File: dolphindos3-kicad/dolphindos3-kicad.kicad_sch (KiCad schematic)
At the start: 23 parts, among them CN1 MB_CPU, CN2 parallel0, IC1 6502, IC10 74LS08, IC2 27256, IC3 6264, IC4 6821, IC5 74LS08, IC6 74LS08, IC7 74LS32, IC8 74LS04, IC9 74LS32

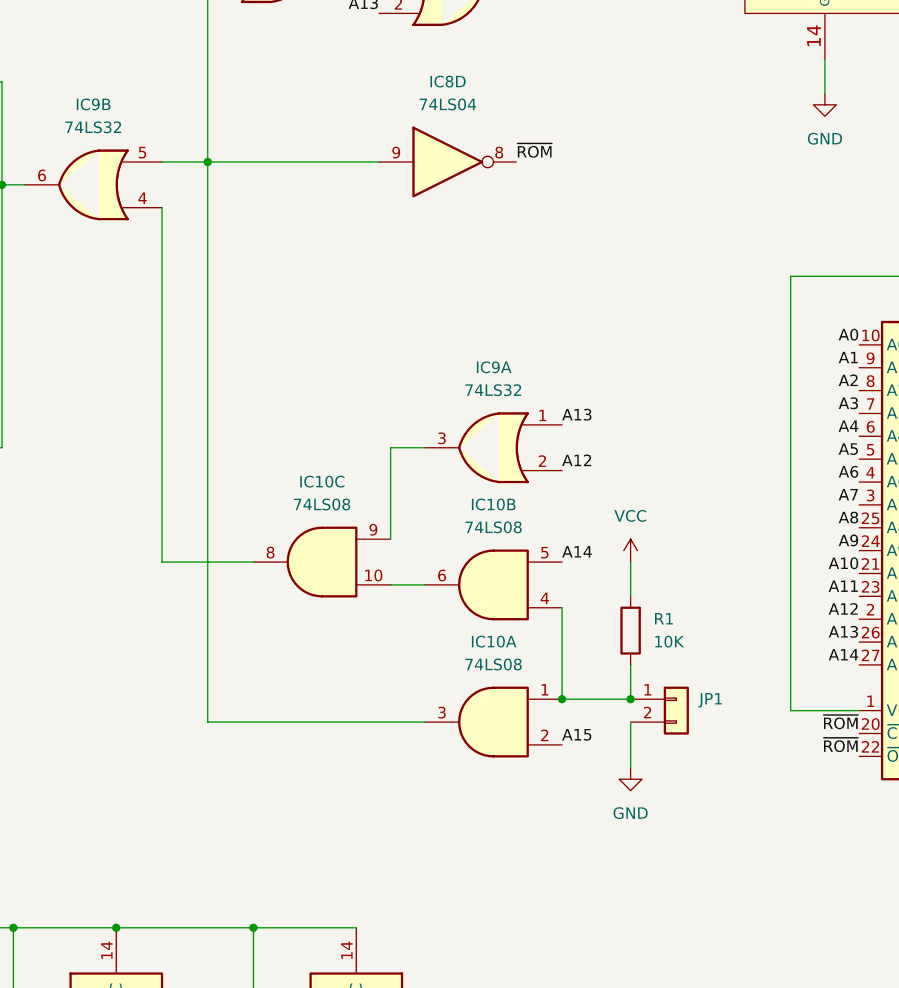
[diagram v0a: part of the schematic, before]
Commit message: redraw without crossed lines
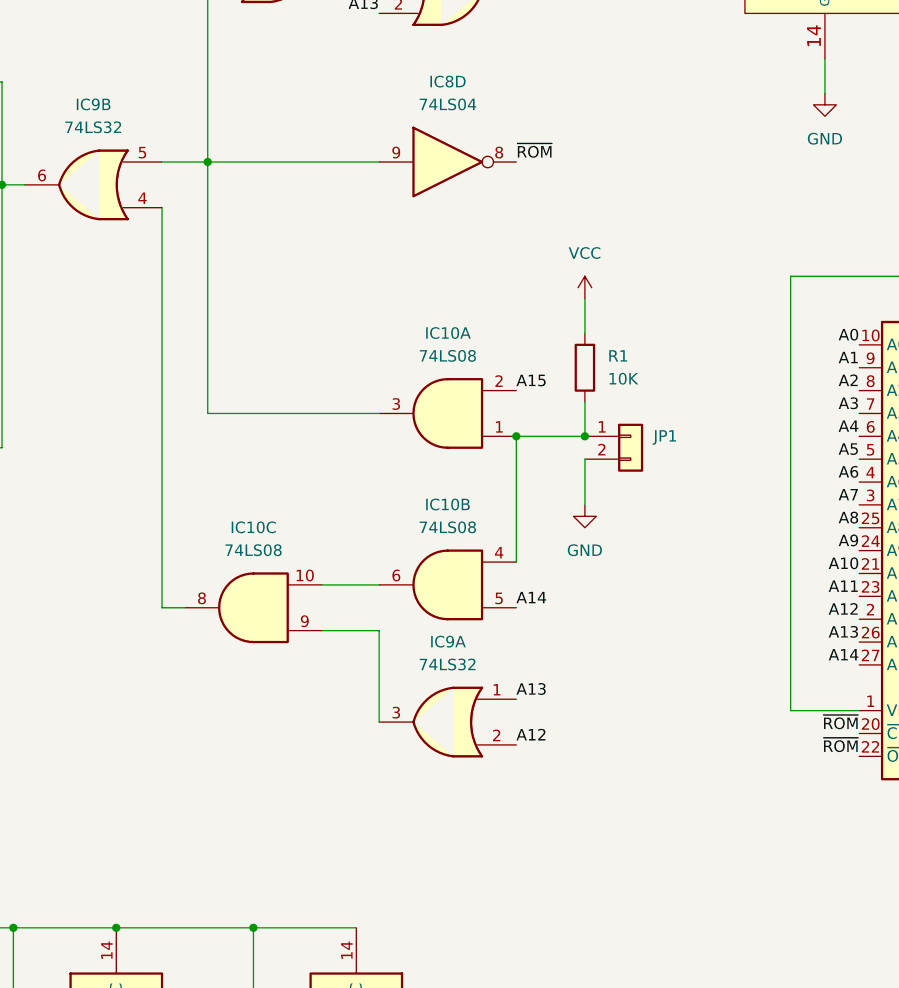
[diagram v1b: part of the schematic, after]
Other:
- moved on the sheet: IC10A, IC10B, IC10C, IC9A, JP1, R1

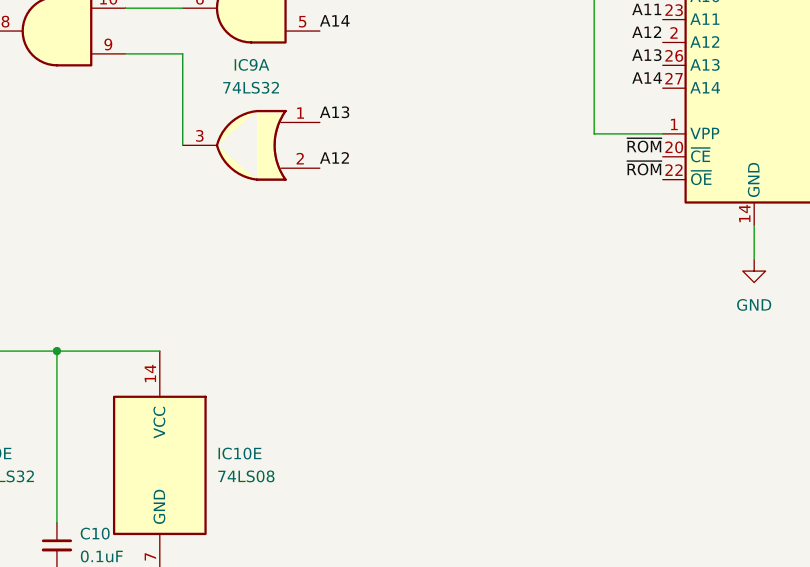
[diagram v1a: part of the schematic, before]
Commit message: IDC socket for parallel cable, added JP2 for drive reset to match gerbers
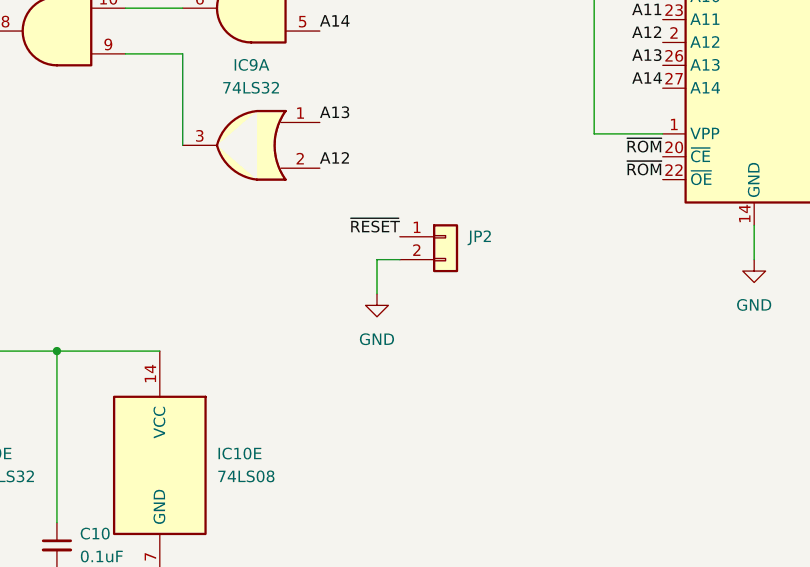
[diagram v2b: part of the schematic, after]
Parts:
- added JP2: Conn_01x02, Connector_PinHeader_2.54mm:PinHeader_1x02_P2.54mm_Vertical, symbol Connector_Generic:Conn_01x02
- CN2: footprint Connector_PinHeader_2.54mm:PinHeader_2x05_P2.54mm_Vertical -> Connector_IDC:IDC-Header_2x05_P2.54mm_Vertical
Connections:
- net GND: now also JP2.2 (Pin_2)
- net ~{RESET}: now also JP2.1 (Pin_1)
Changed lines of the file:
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@@
+    (stroke (width 0) (type default) (color 0 0 0 0))
+  )
+  (wire (pts (xy 186.69 154.94) (xy 189.23 154.94))
     (stroke (width 0) (type default) (color 0 0 0 0))
   )
@@
     (stroke (width 0) (type default) (color 0 0 0 0))
   )
+  (wire (pts (xy 186.69 158.75) (xy 186.69 154.94))
+    (stroke (width 0) (type default) (color 0 0 0 0))
+  )
   (wire (pts (xy 107.95 147.32) (xy 107.95 132.08))
     (stroke (width 0) (type default) (color 0 0 0 0))
@@
   (label "A12" (at 69.85 80.01 0)
     (effects (font (size 1.27 1.27)) (justify left bottom))
+  )
+  (label "~{RESET}" (at 189.23 152.4 180)
+    (effects (font (size 1.27 1.27)) (justify right bottom))
   )
   (label "A10" (at 97.79 81.28 0)
@@
     (pin "7")
   )
+  (symbol (lib_id "power:GND") (at 186.69 158.75 0) (unit 1)
+    (in_bom yes) (on_board yes) (fields_autoplaced)
+    (property "Reference" "#PWR?" (id 0) (at 186.69 165.1 0)
+      (effects (font (size 1.27 1.27)) hide)
+    )
+    (property "Value" "GND" (id 1) (at 186.69 163.83 0))
+    (property "Footprint" "" (id 2) (at 186.69 158.75 0)
+      (effects (font (size 1.27 1.27)) hide)
+    )
+    (property "Datasheet" "" (id 3) (at 186.69 158.75 0)
+      (effects (font (size 1.27 1.27)) hide)
+    )
+    (pin "1")
+  )
   (symbol (lib_id "74xx:74LS08") (at 172.72 127 0) (mirror y) (unit 2)
     (in_bom yes) (on_board yes) (fields_autoplaced)
@@
     (property "Reference" "CN2" (id 0) (at 254 49.53 0))
     (property "Value" "parallel0" (id 1) (at 254 52.07 0))
-    (property "Footprint" "Connector_PinHeader_2.54mm:PinHeader_2x05_P2.54mm_Vertical" (id 2) (at 252.73 60.96 0)
+    (property "Footprint" "Connector_IDC:IDC-Header_2x05_P2.54mm_Vertical" (id 2) (at 252.73 60.96 0)
       (effects (font (size 1.27 1.27)) hide)
     )
@@
     )
     (property "Datasheet" "~" (id 3) (at 124.46 186.69 0)
+      (effects (font (size 1.27 1.27)) hide)
+    )
+    (pin "1")
+    (pin "2")
+  )
+  (symbol (lib_id "Connector_Generic:Conn_01x02") (at 194.31 152.4 0) (unit 1)
+    (in_bom yes) (on_board yes) (fields_autoplaced)
+    (property "Reference" "JP2" (id 0) (at 196.85 152.3999 0)
+      (effects (font (size 1.27 1.27)) (justify left))
+    )
+    (property "Value" "Conn_01x02" (id 1) (at 196.85 154.9399 0)
+      (effects (font (size 1.27 1.27)) (justify left) hide)
+    )
+    (property "Footprint" "Connector_PinHeader_2.54mm:PinHeader_1x02_P2.54mm_Vertical" (id 2) (at 194.31 152.4 0)
+      (effects (font (size 1.27 1.27)) hide)
+    )
+    (property "Datasheet" "~" (id 3) (at 194.31 152.4 0)
       (effects (font (size 1.27 1.27)) hide)
     )
@@
       (reference "#PWR017") (unit 1) (value "GND") (footprint "")
     )
+    (path "/007385b2-d51c-494d-8719-5a21f9b367d4"
+      (reference "#PWR?") (unit 1) (value "GND") (footprint "")
+    )
     (path "/b45e8a50-c3e3-47a9-86e1-69049b92f328"
       (reference "C2") (unit 1) (value "0.1uF") (footprint "Capacitor_THT:C_Disc_D3.4mm_W2.1mm_P2.50mm")
@@
     )
     (path "/5daa3057-3725-4c9c-b9e5-296fec958427"
-      (reference "CN2") (unit 1) (value "parallel0") (footprint "Connector_PinHeader_2.54mm:PinHeader_2x05_P2.54mm_Vertical")
+      (reference "CN2") (unit 1) (value "parallel0") (footprint "Connector_IDC:IDC-Header_2x05_P2.54mm_Vertical")
     )
     (path "/a89de2f7-3bfc-4c06-8b94-fa5ab5669397"
@@
       (reference "JP1") (unit 1) (value "Conn_01x02") (footprint "Connector_PinHeader_2.54mm:PinHeader_1x02_P2.54mm_Vertical")
     )
+    (path "/6daaca7d-5073-458f-8650-5fc3b99c3b46"
+      (reference "JP2") (unit 1) (value "Conn_01x02") (footprint "Connector_PinHeader_2.54mm:PinHeader_1x02_P2.54mm_Vertical")
+    )
     (path "/17489be5-e61f-4226-aa74-51e1fb710772"

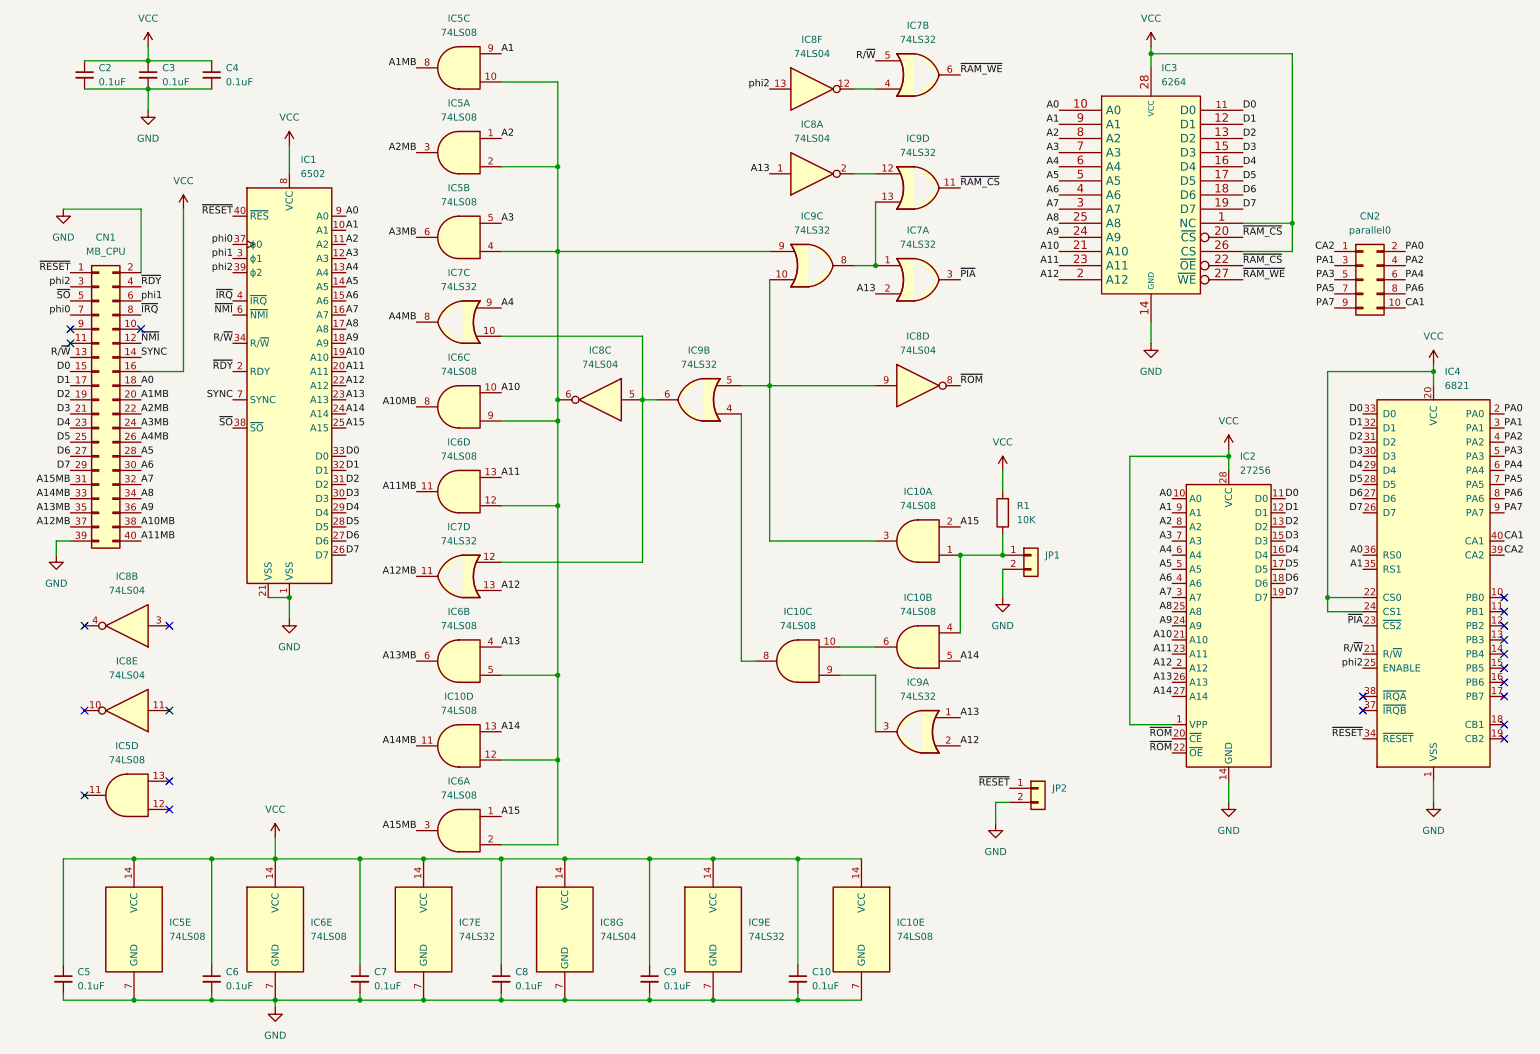
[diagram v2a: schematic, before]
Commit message: mods: RAM A13/14 from PIA PB, ROM A15, unused gate inputs tied to GND pcb: autorouted, parts moved for C128DCR plug-in option
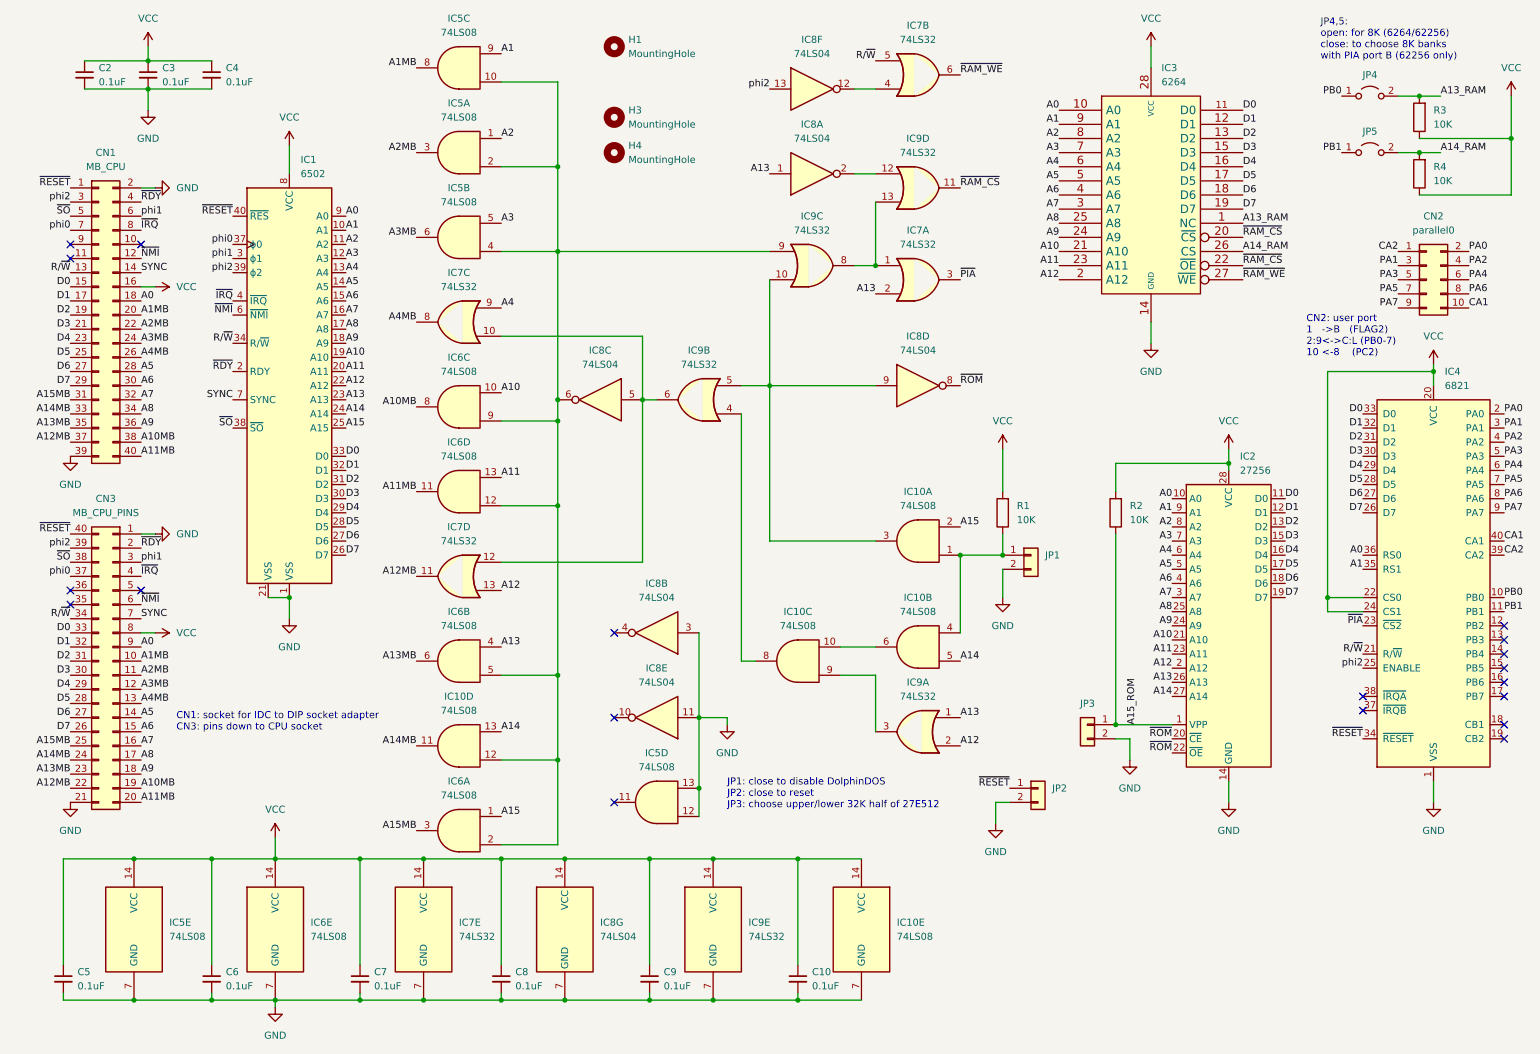
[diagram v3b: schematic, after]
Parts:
- added CN3: MB_CPU_PINS, Package_DIP:DIP-40_W15.24mm, symbol Connector_Generic:Conn_02x20_Counter_Clockwise
- added H1, H3, H4: MountingHole, MountingHole:MountingHole_3mm, symbol Mechanical:MountingHole
- added JP3: Conn_01x02, Connector_PinHeader_2.54mm:PinHeader_1x02_P2.54mm_Vertical, symbol Connector_Generic:Conn_01x02
- added JP4, JP5: Jumper_2_Open, Connector_PinHeader_2.54mm:PinHeader_1x02_P2.54mm_Vertical, symbol Jumper:Jumper_2_Open
- added R2, R3, R4: 10K, Resistor_THT:R_Axial_DIN0207_L6.3mm_D2.5mm_P7.62mm_Horizontal, symbol Device:R
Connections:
- net A0: now also CN3.9 (Pin_9)
- net A10MB: now also CN3.19 (Pin_19)
- net A11MB: now also CN3.20 (Pin_20)
- net A12MB: now also CN3.22 (Pin_22)
- net A13MB: now also CN3.23 (Pin_23)
- net A14MB: now also CN3.24 (Pin_24)
- net A15MB: now also CN3.25 (Pin_25)
- net A1MB: now also CN3.10 (Pin_10)
- net A2MB: now also CN3.11 (Pin_11)
- net A3MB: now also CN3.12 (Pin_12)
- net A4MB: now also CN3.13 (Pin_13)
- net A5: now also CN3.14 (Pin_14)
- net A6: now also CN3.15 (Pin_15)
- net A7: now also CN3.16 (Pin_16)
- net A8: now also CN3.17 (Pin_17)
- net A9: now also CN3.18 (Pin_18)
- net D0: now also CN3.33 (Pin_33)
- net D1: now also CN3.32 (Pin_32)
- net D2: now also CN3.31 (Pin_31)
- net D3: now also CN3.30 (Pin_30)
- net D4: now also CN3.29 (Pin_29)
- net D5: now also CN3.28 (Pin_28)
- net D6: now also CN3.27 (Pin_27)
- net D7: now also CN3.26 (Pin_26)
- net GND: now also IC5.12, IC5.13, IC8.11, IC8.3, CN3.1 (Pin_1), CN3.21 (Pin_21), JP3.2 (Pin_2)
- net R/~{W}: now also CN3.34 (Pin_34)
- net SYNC: now also CN3.7 (Pin_7)
- net VCC: now also CN3.8 (Pin_8), R2.2, R3.1, R4.1; no longer IC2.1 (VPP), IC3.1 (NC), IC3.26 (CS)
- net phi0: now also CN3.37 (Pin_37)
- net phi1: now also CN3.3 (Pin_3)
- net phi2: now also CN3.39 (Pin_39)
- net ~{IRQ}: now also CN3.4 (Pin_4)
- net ~{NMI}: now also CN3.6 (Pin_6)
- net ~{RDY}: now also CN3.2 (Pin_2)
- net ~{RESET}: now also CN3.40 (Pin_40)
- net ~{SO}: now also CN3.38 (Pin_38)
- net PB0: now reaches IC4.10 (PB0)
- net PB0: now also JP4.1 (A)
- net PB1: now reaches IC4.11 (PB1)
- net PB1: now also JP5.1 (A)
- new net A13_RAM: IC3.1 (NC), JP4.2 (B), R3.2
- new net A14_RAM: IC3.26 (CS), JP5.2 (B), R4.2
- new net A15_ROM: IC2.1 (VPP), JP3.1 (Pin_1), R2.1
- no-connect marks 22 -> 19
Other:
- note added: "CN1: socket for IDC to DIP socket adapter CN3: pins down to CPU socket"
- note added: "CN2: user port 1 ->B (FLAG2) 2:9<->C:L (PB0-7) 10 <-8 (PC2)"
- note added: "JP1: close to disable DolphinDOS JP2: close to reset JP3: choose upper/lower 32K half of 27E512"
- note added: "JP4,5: open: for 8K (6264/62256) close: to choose 8K banks with PIA port B (62256 only)"
- moved on the sheet: CN1, CN2, IC5D, IC8B, IC8E
